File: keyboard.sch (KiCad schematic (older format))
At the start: 18 parts, among them IC1 ATMEGA32U4, J1 USBMINI_B05, P1 ISP, P2 GPIO Port, X1 CRYSTAL

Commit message: Final touches on schematic & Clean up PCB
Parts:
- IC1: footprint tqfp:TQFP44 -> Housings_QFP:TQFP-44_10x10mm_Pitch0.8mm
- P2: footprint (none) -> Socket_Strips:Socket_Strip_Straight_1x04
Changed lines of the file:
@@
 Sheet 1 3
 Title ""
-Date ""
+Date "CW40_2.0"
 Rev ""
 Comp ""
@@
 F 0 "IC1" H 4250 6180 50  0000 L BNN
 F 1 "ATMEGA32U4" H 5300 2450 50  0000 L BNN
-F 2 "tqfp:TQFP44" H 5550 2375 50  0001 C CNN
+F 2 "Housings_QFP:TQFP-44_10x10mm_Pitch0.8mm" H 5550 2375 50  0001 C CNN
 F 3 "" H 5050 4350 60  0000 C CNN
 	1    5050 4350
@@
 F 0 "P2" V 9250 1700 50  0000 C CNN
 F 1 "GPIO Port" V 9350 1700 50  0000 C CNN
-F 2 "" H 9300 1700 60  0000 C CNN
+F 2 "Socket_Strips:Socket_Strip_Straight_1x04" H 9300 1700 60  0001 C CNN
 F 3 "" H 9300 1700 60  0000 C CNN
 	1    9300 1700

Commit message: Layout
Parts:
- removed S0: DTSM-6, switch:DTSM-6, symbol DTSM-6
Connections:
- wire segments 118 -> 116
- no-connect marks 4 -> 2
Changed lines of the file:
@@
 NoConn ~ 4050 4550
-$Comp
-L GND #PWR02
-U 1 1 573FF693
-P 2400 2800
-F 0 "#PWR02" H 2400 2800 30  0001 C CNN
-F 1 "GND" H 2400 2730 30  0001 C CNN
-F 2 "" H 2400 2800 60  0000 C CNN
-F 3 "" H 2400 2800 60  0000 C CNN
-	1    2400 2800
-	1    0    0    -1
-$EndComp
-$Comp
-L DTSM-6 S0
-U 1 1 573FF79F
-P 2850 2650
-F 0 "S0" V 2565 2550 50  0000 L BNN
-F 1 "DTSM-6" V 2665 2775 50  0000 L BNN
-F 2 "switch:DTSM-6" H 2850 2800 50  0001 C CNN
-F 3 "" H 2850 2650 60  0000 C CNN
-	1    2850 2650
-	0    1    1    0
-$EndComp
 $Comp
 L R R5
@@
 $EndComp
 $Comp
-L VCC #PWR03
+L VCC #PWR02
 U 1 1 573FFE51
 P 3700 950
-F 0 "#PWR03" H 3700 1050 30  0001 C CNN
+F 0 "#PWR02" H 3700 1050 30  0001 C CNN
 F 1 "VCC" H 3700 1050 30  0000 C CNN
 F 2 "" H 3700 950 60  0000 C CNN
@@
 $EndComp
 $Comp
-L VCC #PWR04
+L VCC #PWR03
 U 1 1 57400628
 P 5250 2050
-F 0 "#PWR04" H 5250 2150 30  0001 C CNN
+F 0 "#PWR03" H 5250 2150 30  0001 C CNN
 F 1 "VCC" H 5250 2150 30  0000 C CNN
 F 2 "" H 5250 2050 60  0000 C CNN
@@
 $EndComp
 $Comp
-L VCC #PWR05
+L VCC #PWR04
 U 1 1 5740064C
 P 5150 2050
-F 0 "#PWR05" H 5150 2150 30  0001 C CNN
+F 0 "#PWR04" H 5150 2150 30  0001 C CNN
 F 1 "VCC" H 5150 2150 30  0000 C CNN
 F 2 "" H 5150 2050 60  0000 C CNN
@@
 $EndComp
 $Comp
-L VCC #PWR06
+L VCC #PWR05
 U 1 1 57400669
 P 4950 2050
-F 0 "#PWR06" H 4950 2150 30  0001 C CNN
+F 0 "#PWR05" H 4950 2150 30  0001 C CNN
 F 1 "VCC" H 4950 2150 30  0000 C CNN
 F 2 "" H 4950 2050 60  0000 C CNN
@@
 $EndComp
 $Comp
-L VCC #PWR07
+L VCC #PWR06
 U 1 1 57400686
 P 4850 2050
-F 0 "#PWR07" H 4850 2150 30  0001 C CNN
+F 0 "#PWR06" H 4850 2150 30  0001 C CNN
 F 1 "VCC" H 4850 2150 30  0000 C CNN
 F 2 "" H 4850 2050 60  0000 C CNN
@@
 $EndComp
 $Comp
-L VCC #PWR08
+L VCC #PWR07
 U 1 1 574019E0
 P 3000 4950
-F 0 "#PWR08" H 3000 5050 30  0001 C CNN
+F 0 "#PWR07" H 3000 5050 30  0001 C CNN
 F 1 "VCC" H 3000 5050 30  0000 C CNN
 F 2 "" H 3000 4950 60  0000 C CNN
@@
 NoConn ~ 2900 5400
 $Comp
-L GND #PWR09
+L GND #PWR08
 U 1 1 57401AD9
 P 3000 5700
-F 0 "#PWR09" H 3000 5700 30  0001 C CNN
+F 0 "#PWR08" H 3000 5700 30  0001 C CNN
 F 1 "GND" H 3000 5630 30  0001 C CNN
 F 2 "" H 3000 5700 60  0000 C CNN
@@
 $EndComp
 $Comp
-L VCC #PWR010
+L VCC #PWR09
 U 1 1 57402200
 P 3900 4850
-F 0 "#PWR010" H 3900 4950 30  0001 C CNN
+F 0 "#PWR09" H 3900 4950 30  0001 C CNN
 F 1 "VCC" H 3900 4950 30  0000 C CNN
 F 2 "" H 3900 4850 60  0000 C CNN
@@
 $EndComp
 $Comp
-L GND #PWR011
+L GND #PWR010
 U 1 1 57402590
 P 4000 6250
-F 0 "#PWR011" H 4000 6250 30  0001 C CNN
+F 0 "#PWR010" H 4000 6250 30  0001 C CNN
 F 1 "GND" H 4000 6180 30  0001 C CNN
 F 2 "" H 4000 6250 60  0000 C CNN
@@
 $EndComp
 $Comp
-L GND #PWR012
+L GND #PWR011
 U 1 1 5740267C
 P 3750 6250
-F 0 "#PWR012" H 3750 6250 30  0001 C CNN
+F 0 "#PWR011" H 3750 6250 30  0001 C CNN
 F 1 "GND" H 3750 6180 30  0001 C CNN
 F 2 "" H 3750 6250 60  0000 C CNN
@@
 $EndComp
 $Comp
-L GND #PWR013
+L GND #PWR012
 U 1 1 57402D78
 P 4900 6550
-F 0 "#PWR013" H 4900 6550 30  0001 C CNN
+F 0 "#PWR012" H 4900 6550 30  0001 C CNN
 F 1 "GND" H 4900 6480 30  0001 C CNN
 F 2 "" H 4900 6550 60  0000 C CNN
@@
 $EndComp
 $Comp
-L GND #PWR014
+L GND #PWR013
 U 1 1 57402EAD
 P 5000 6550
-F 0 "#PWR014" H 5000 6550 30  0001 C CNN
+F 0 "#PWR013" H 5000 6550 30  0001 C CNN
 F 1 "GND" H 5000 6480 30  0001 C CNN
 F 2 "" H 5000 6550 60  0000 C CNN
@@
 $EndComp
 $Comp
-L GND #PWR015
+L GND #PWR014
 U 1 1 57402FDC
 P 5100 6550
-F 0 "#PWR015" H 5100 6550 30  0001 C CNN
+F 0 "#PWR014" H 5100 6550 30  0001 C CNN
 F 1 "GND" H 5100 6480 30  0001 C CNN
 F 2 "" H 5100 6550 60  0000 C CNN
@@
 $EndComp
 $Comp
-L GND #PWR016
+L GND #PWR015
 U 1 1 5740303A
 P 5200 6550
-F 0 "#PWR016" H 5200 6550 30  0001 C CNN
+F 0 "#PWR015" H 5200 6550 30  0001 C CNN
 F 1 "GND" H 5200 6480 30  0001 C CNN
 F 2 "" H 5200 6550 60  0000 C CNN
@@
 $EndComp
 $Comp
-L GND #PWR017
+L GND #PWR016
 U 1 1 57403AAC
 P 6150 6550
-F 0 "#PWR017" H 6150 6550 30  0001 C CNN
+F 0 "#PWR016" H 6150 6550 30  0001 C CNN
 F 1 "GND" H 6150 6480 30  0001 C CNN
 F 2 "" H 6150 6550 60  0000 C CNN
@@
 	3500 4050 3500 4200
 Connection ~ 3500 4050
-Wire Wire Line
-	2400 2650 2400 2800
-Wire Wire Line
-	2400 2650 2650 2650
-Wire Wire Line
-	3050 2650 4050 2650
-Connection ~ 3700 2650
 Wire Wire Line
 	3700 1550 4850 1550
@@
 	5900 1350 5900 1250
 $Comp
-L VCC #PWR018
+L VCC #PWR017
 U 1 1 57835D2A
 P 5900 1250
-F 0 "#PWR018" H 5900 1350 30  0001 C CNN
+F 0 "#PWR017" H 5900 1350 30  0001 C CNN
 F 1 "VCC" H 5900 1350 30  0000 C CNN
 F 2 "" H 5900 1250 60  0000 C CNN
@@
 	5900 1550 5900 1650
 $Comp
-L GND #PWR019
+L GND #PWR018
 U 1 1 57838F38
 P 5900 1650
-F 0 "#PWR019" H 5900 1650 30  0001 C CNN
+F 0 "#PWR018" H 5900 1650 30  0001 C CNN
 F 1 "GND" H 5900 1580 30  0001 C CNN
 F 2 "" H 5900 1650 60  0000 C CNN
@@
 	1    0    0    -1
 $EndComp
-NoConn ~ 2650 2750
-NoConn ~ 3050 2750
 Wire Wire Line
 	700  1050 1900 1050
@@
 Connection ~ 1600 1750
 $Comp
-L VCC #PWR020
+L VCC #PWR019
 U 1 1 578E955E
 P 1300 900
-F 0 "#PWR020" H 1300 1000 30  0001 C CNN
+F 0 "#PWR019" H 1300 1000 30  0001 C CNN
 F 1 "VCC" H 1300 1000 30  0000 C CNN
 F 2 "" H 1300 900 60  0000 C CNN
@@
 $EndComp
 $Comp
-L GND #PWR021
+L GND #PWR020
 U 1 1 578EF284
 P 1300 1900
-F 0 "#PWR021" H 1300 1900 30  0001 C CNN
+F 0 "#PWR020" H 1300 1900 30  0001 C CNN
 F 1 "GND" H 1300 1830 30  0001 C CNN
 F 2 "" H 1300 1900 60  0000 C CNN
@@
 Text Label 8350 1900 0    60   ~ 0
 GPIO4
+Wire Wire Line
+	3700 2650 4050 2650
 $EndSCHEMATC

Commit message: rebuild daisy
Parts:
- P1: footprint Socket_Strips:Socket_Strip_Straight_2x03 -> Socket_Strips:Socket_Strip_Straight_2x03_Pitch2.54mm
- P2: footprint Socket_Strips:Socket_Strip_Straight_1x04 -> Socket_Strips:Socket_Strip_Straight_1x05_Pitch2.54mm
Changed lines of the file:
@@
 F 0 "P1" H 5250 1750 50  0000 C CNN
 F 1 "ISP" V 5250 1550 40  0000 C CNN
-F 2 "Socket_Strips:Socket_Strip_Straight_2x03" H 5250 1500 60  0001 C CNN
+F 2 "Socket_Strips:Socket_Strip_Straight_2x03_Pitch2.54mm" H 5250 1500 60  0001 C CNN
 F 3 "" H 5250 1500 60  0000 C CNN
 	1    5250 1500
@@
 F 0 "P2" V 9250 1700 50  0000 C CNN
 F 1 "GPIO Port" V 9350 1700 50  0000 C CNN
-F 2 "Socket_Strips:Socket_Strip_Straight_1x04" H 9300 1700 60  0001 C CNN
+F 2 "Socket_Strips:Socket_Strip_Straight_1x05_Pitch2.54mm" H 9300 1700 60  0001 C CNN
 F 3 "" H 9300 1700 60  0000 C CNN
 	1    9300 1700

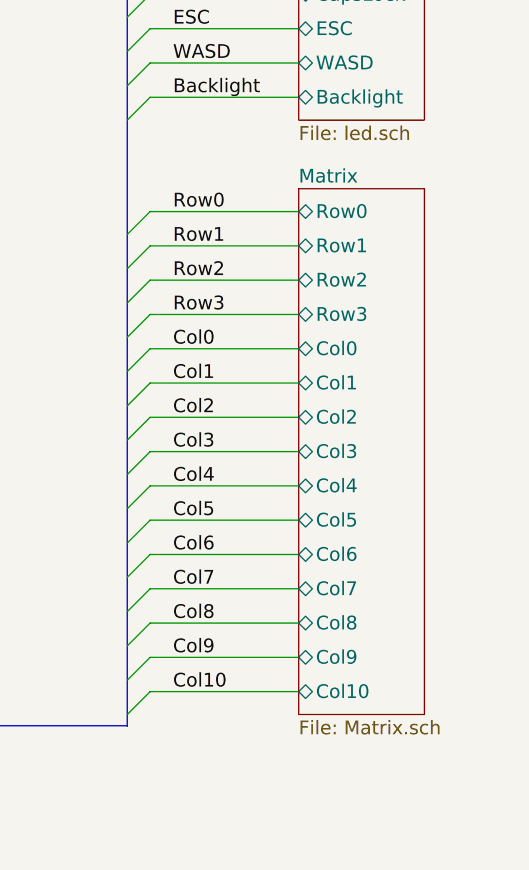
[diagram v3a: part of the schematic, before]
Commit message: Adjust logo and version information
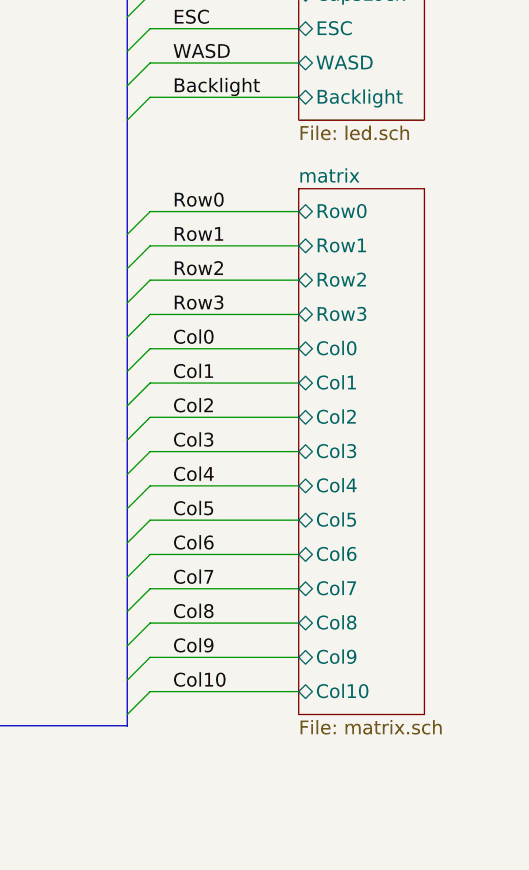
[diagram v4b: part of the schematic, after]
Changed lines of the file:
@@
 encoding utf-8
 Sheet 1 3
-Title ""
-Date "CW40_2.0"
-Rev ""
-Comp ""
+Title "Daisy"
+Date "2017-05-08"
+Rev "v0.1a"
+Comp "K.T.E.C."
 Comment1 ""
 Comment2 ""
@@
 S 8900 3750 550  2300
 U 57404552
-F0 "Matrix" 60
-F1 "Matrix.sch" 60
+F0 "matrix" 60
+F1 "matrix.sch" 60
 F2 "Row0" B L 8900 3850 60
 F3 "Row1" B L 8900 4000 60

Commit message: Redesign v0.3
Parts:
- removed R3: 10K, Resistors_SMD:R_0805, symbol R
- added C10, C4: 100nF, capacitors:C_0805, symbol C
- added DA1: WE05-4RVLCH, diodes:SOT-23-6_Handsoldering, symbol WE05-4RVLCH
- added JP1, JP2: JUMPER, passives:Jumper_SMD_2Pads_NC_V, symbol JUMPER
- added P3: GPIO_CLUSTER2, connectors:Socket_Strip_Straight_1x04_Pitch2.54mm, symbol CONN_01X04
- added R6, R7: 4.7K, resistors:R_0805_NA, symbol R
- C1, C2, C3: footprint Capacitors_SMD:C_0805 -> capacitors:C_0805
- C5: renamed from C8; footprint Capacitors_SMD:C_0805 -> capacitors:C_0805
- C6: renamed from C4; footprint Capacitors_SMD:C_0805 -> capacitors:C_0805
- C7: renamed from C5; footprint Capacitors_SMD:C_0805 -> capacitors:C_0805
- C8: renamed from C6; footprint Capacitors_SMD:C_0805 -> capacitors:C_0805
- C9: renamed from C7; footprint Capacitors_SMD:C_0805 -> capacitors:C_0805
- J1: value USBMINI_B05 -> USB_MINI-B; footprint USB:DX_USB -> connectors:USB_MINI-B; symbol USBMINI_B05 -> USB_MINI-B
- P1: footprint Socket_Strips:Socket_Strip_Straight_2x03_Pitch2.54mm -> connectors:Socket_Strip_Straight_1x06_Pitch2.54mm; symbol CONN_3X2 -> CONN_02X03
- P2: value GPIO Port -> GPIO_CLUSTER1; footprint Socket_Strips:Socket_Strip_Straight_1x05_Pitch2.54mm -> connectors:Socket_Strip_Straight_2x04_Pitch2.54mm; symbol CONN_5 -> CONN_02X04
- R1, R2: footprint Resistors_SMD:R_0805 -> resistors:R_0805_V1
- R5: footprint Resistors_SMD:R_0805 -> resistors:R_0805
- U1: renamed from IC1; footprint Housings_QFP:TQFP-44_10x10mm_Pitch0.8mm -> housings:TQFP44+QFN44
- X1: footprint Crystals:Crystal_HC49-U_Vertical -> Crystals:Crystal_SMD_5032-2pin_5.0x3.2mm; symbol CRYSTAL -> Crystal
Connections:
- net labels added: Esc, GPIO5, GPIO6, GPIO7, RGB, SHIELD, ~RESET
- net labels removed: Bottom, ESC, WASD, ~Res
- wire segments 116 -> 150
- no-connect marks 2 -> 3
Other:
- moved on the sheet: P1, R1, R2, R5

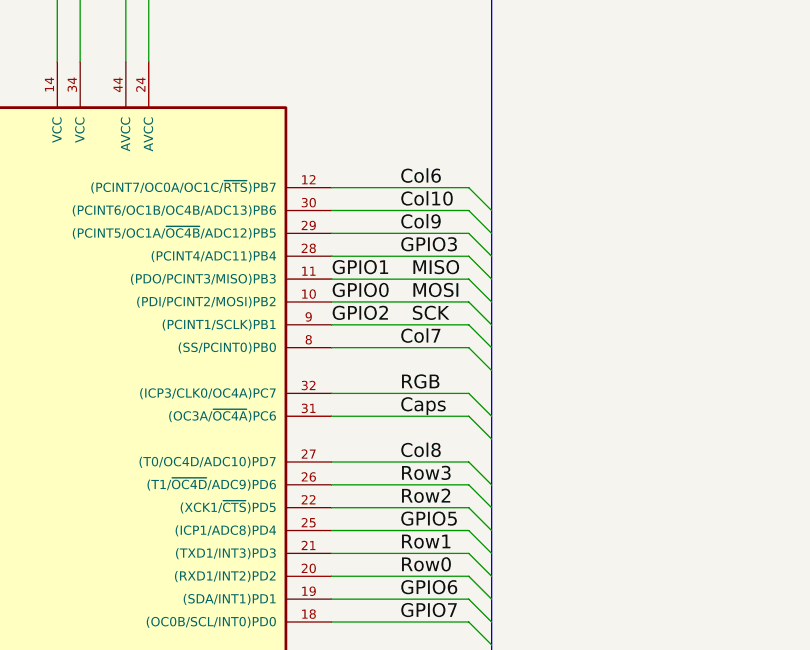
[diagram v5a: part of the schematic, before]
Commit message: Change to v0.4 - Change pin assignment - Change logos
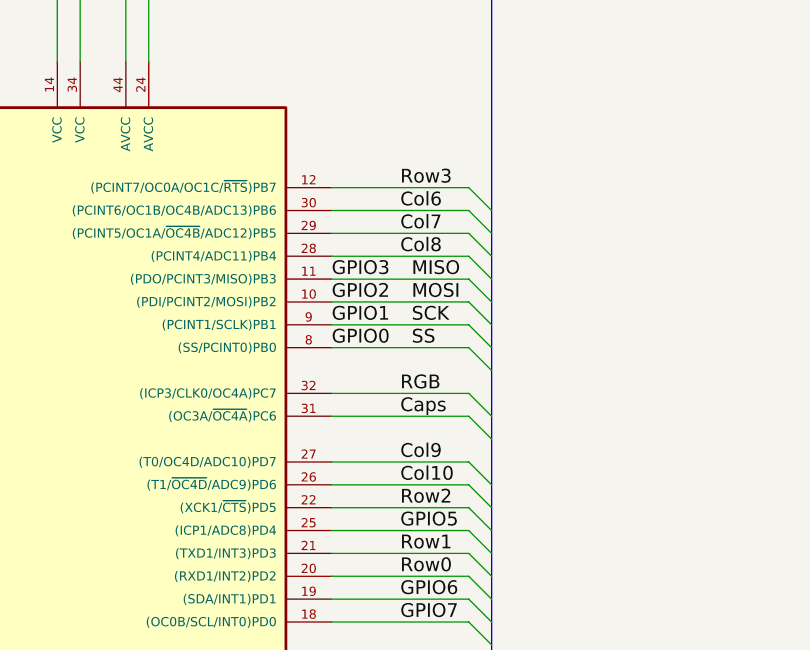
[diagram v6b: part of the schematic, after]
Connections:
- net Col10: now also U1.26 ((T1/~OC4D~/ADC9)PD6); no longer U1.30 ((PCINT6/OC1B/OC4B/ADC13)PB6)
- net Col6: now also U1.30 ((PCINT6/OC1B/OC4B/ADC13)PB6); no longer U1.12 ((PCINT7/OC0A/OC1C/~RTS~)PB7)
- net Col7: now also U1.29 ((PCINT5/OC1A/~OC4B~/ADC12)PB5); no longer U1.8 ((SS/PCINT0)PB0)
- net Col8: now also U1.28 ((PCINT4/ADC11)PB4); no longer U1.27 ((T0/OC4D/ADC10)PD7)
- net Col9: now also U1.27 ((T0/OC4D/ADC10)PD7); no longer U1.29 ((PCINT5/OC1A/~OC4B~/ADC12)PB5)
- net GPIO0: now also U1.8 ((SS/PCINT0)PB0); no longer P1.4 (P4), U1.10 ((PDI/PCINT2/MOSI)PB2)
- net GPIO1: now also P1.3 (P3), U1.9 ((PCINT1/SCLK)PB1); no longer P1.1 (P1), U1.11 ((PDO/PCINT3/MISO)PB3)
- net GPIO2: now also P1.4 (P4), U1.10 ((PDI/PCINT2/MOSI)PB2); no longer P1.3 (P3), U1.9 ((PCINT1/SCLK)PB1)
- net GPIO3: now also P1.1 (P1), U1.11 ((PDO/PCINT3/MISO)PB3); no longer U1.28 ((PCINT4/ADC11)PB4)
- net Row3: now also U1.12 ((PCINT7/OC0A/OC1C/~RTS~)PB7); no longer U1.26 ((T1/~OC4D~/ADC9)PD6)
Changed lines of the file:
@@
 GPIO4
 Text Label 6350 3200 0    60   ~ 0
-GPIO3
+Col8
 Text Label 6350 4600 0    60   ~ 0
 Row0
@@
 Row2
 Text Label 6350 4200 0    60   ~ 0
-Row3
+Col10
 Text Label 6350 3900 0    60   ~ 0
 Caps
@@
 Text Label 6350 3800 0    60   ~ 0
 RGB
-Text Label 6350 3600 0    60   ~ 0
+Text Label 6050 3600 0    60   ~ 0
+GPIO0
+Text Label 6350 3100 0    60   ~ 0
 Col7
-Text Label 6350 3100 0    60   ~ 0
-Col9
 Text Label 6350 3000 0    60   ~ 0
-Col10
+Col6
 Text Label 6350 2900 0    60   ~ 0
-Col6
+Row3
 Text Label 8350 5350 0    60   ~ 0
 Col6
@@
 MOSI
 Text Label 6050 3500 0    60   ~ 0
+GPIO1
+Text Label 6050 3400 0    60   ~ 0
 GPIO2
-Text Label 6050 3400 0    60   ~ 0
-GPIO0
 Text Label 6400 3300 0    60   ~ 0
 MISO
 Text Label 6350 4100 0    60   ~ 0
-Col8
+Col9
 Entry Wire Line
 	8150 1550 8250 1450
@@
 GPIO7
 Text Label 6050 3300 0    60   ~ 0
-GPIO1
+GPIO3
 Text Label 6400 3400 0    60   ~ 0
 MOSI
@@
 	8950 2050 8950 2300
 Connection ~ 8950 2300
+Text Label 6400 3600 0    60   ~ 0
+SS
 $EndSCHEMATC
